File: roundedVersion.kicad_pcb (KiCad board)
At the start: 2 copper layers, 161.3 x 118.3 mm, 48 parts, among them U1 SuperMini nRF52840

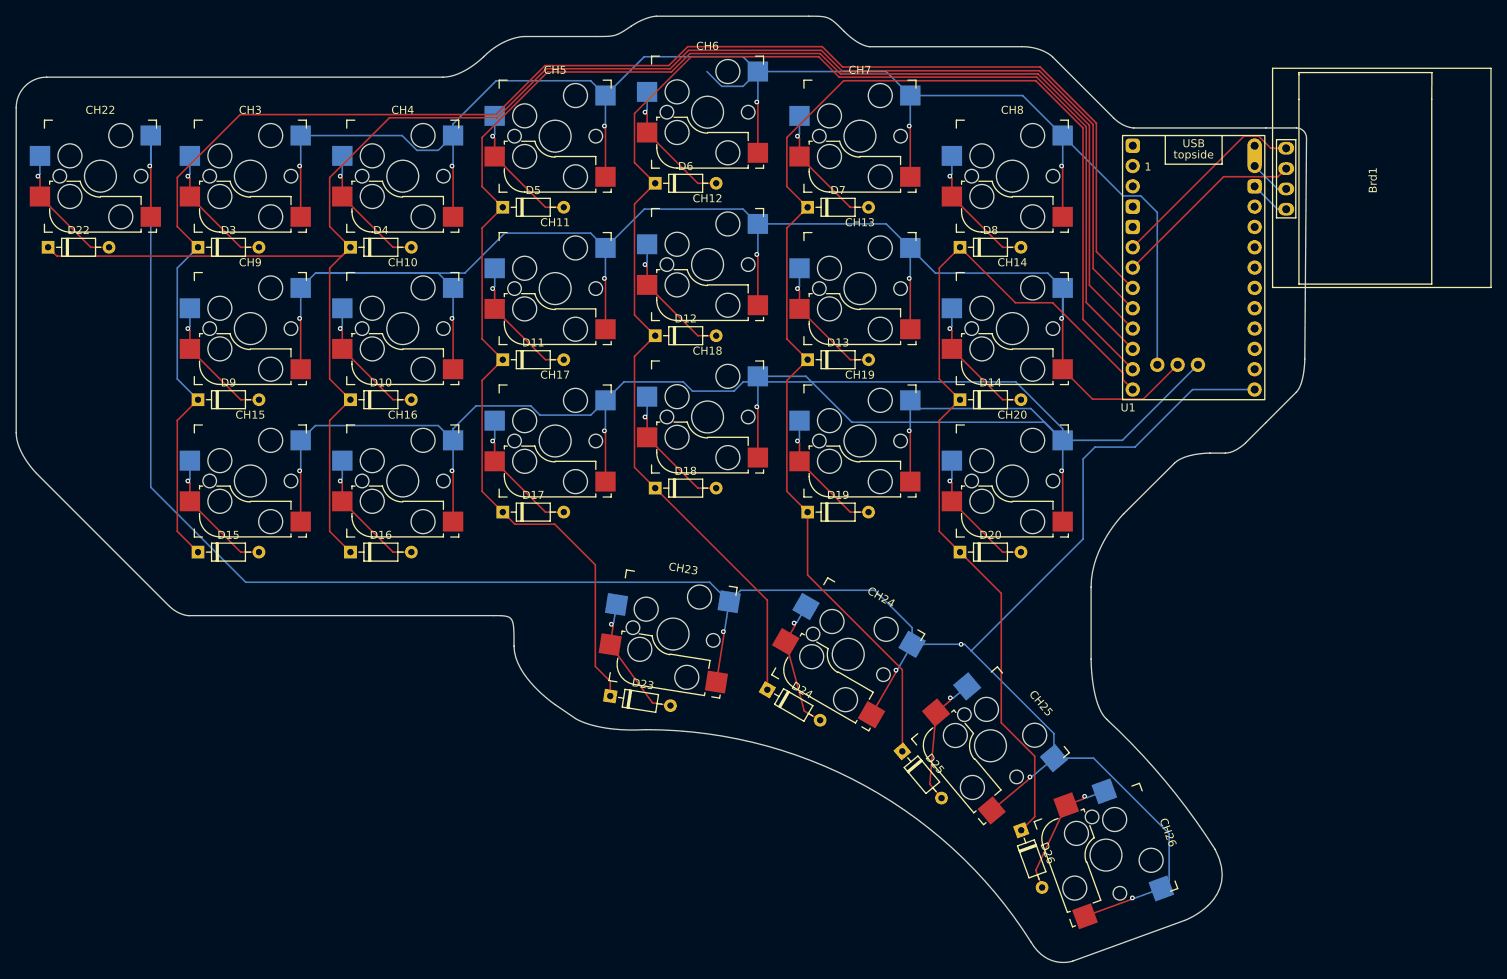
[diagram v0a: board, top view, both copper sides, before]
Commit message: rounded version added
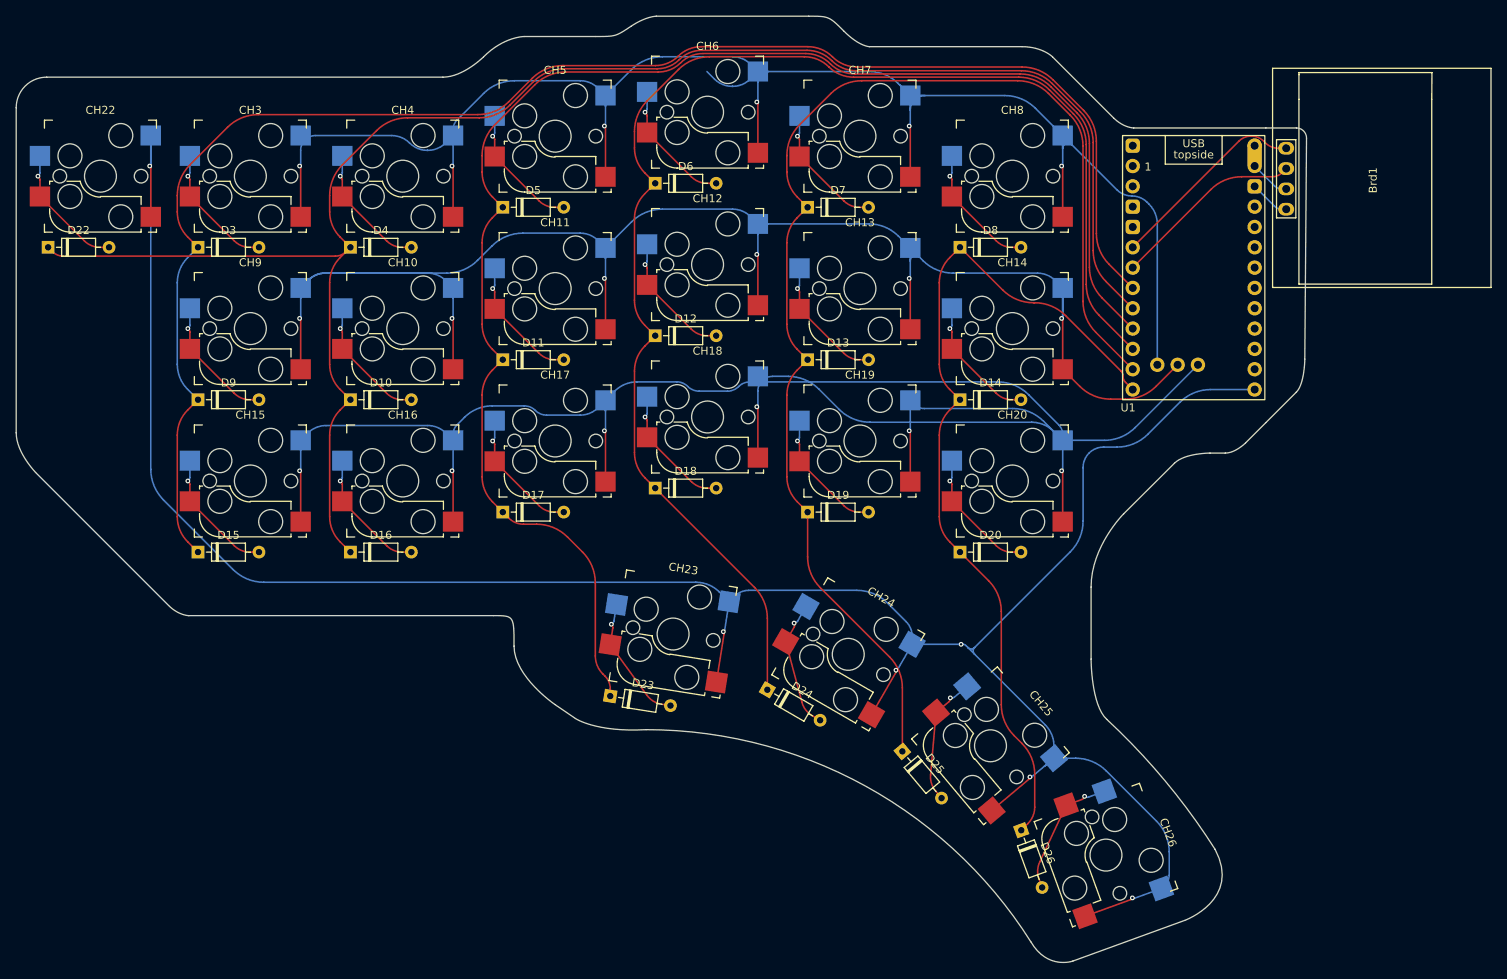
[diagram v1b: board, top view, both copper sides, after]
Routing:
- net Row1: track 211.7 -> 222.0 mm
- net Row2: track 206.2 -> 214.1 mm
- net Col3: track 195.3 -> 191.2 mm
- net Row4: track 306.8 -> 310.7 mm
- net Col2: track 221.8 -> 217.9 mm
- net Col1: track 200.3 -> 196.6 mm
- net Col4: track 176.4 -> 173.4 mm
- net Col5: track 162.1 -> 159.2 mm
- net Col6: track 111.2 -> 108.8 mm
- net Row3: track 251.4 -> 250.6 mm
